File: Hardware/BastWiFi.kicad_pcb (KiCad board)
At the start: 2 copper layers, 50.8 x 22.9 mm, 31 parts, among them J1 Conn_Battery, J2 USB_B_Micro, J3 Conn_Left, J4 Conn_Right, Q1 DMG3415U-7, SW1 GPIO0, SW2 RESET, U1 MCP73831-3-OT, U2 AP2112K-3.3, U3 ESP32-S2-WROVER

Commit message: Change footprint sw
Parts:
- SW1, SW2: footprint Button_Switch_SMD:SW_SPST_TL3342 -> Button_Switch_SMD:SW_SPST_B3U-1000P
- moved REF** 9.87 mm to (185.1, 83.2)
- moved REF** 9.81 mm to (185.1, 102.2)
- moved SW1 5.97 mm to (139.0, 111.5)
- moved SW2 2.81 mm to (144.8, 111.5)
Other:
- board size 50.8 x 22.9 mm -> 60 x 22.9 mm
- net class Default: trace_width 0.25 -> 0.3

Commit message: Tracks
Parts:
- moved R1 19.9 mm to (150.1, 84.6), turned to 180 degrees
- moved SW1 17.1 mm to (136.9, 94.6)
- moved R8 16.7 mm to (141.2, 100.7), turned to 180 degrees
- moved SW2 14.4 mm to (136.9, 99.6)
- moved C6 12.8 mm to (148.0, 99.8), turned to 90 degrees
- moved D2 11.7 mm to (144.3, 88.6)
- moved U1 10.7 mm to (147.9, 87.5)
- moved C7 10.2 mm to (141.2, 99.1)
- moved C2 8.95 mm to (143.9, 93.9), turned to 270 degrees
- moved R6 8.41 mm to (132.2, 99.6), turned to 90 degrees
- moved Q1 7.22 mm to (141.3, 94.4), turned to 270 degrees
- moved U2 6.79 mm to (147.9, 95.7)
- moved C5 6.30 mm to (149.6, 99.8), turned to 90 degrees
- moved R5 6.26 mm to (133.7, 99.6), turned to 90 degrees
- moved R4 6.22 mm to (148.0, 93.1), turned to 180 degrees
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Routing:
- net /~RST~: track 0.00 -> 68.7 mm, vias 0 -> 2
- net /GPIO0: track 0.00 -> 49.5 mm, vias 0 -> 2
- net /SCL: track 0.00 -> 48.3 mm, vias 0 -> 1
- net /SDA: track 0.00 -> 44.5 mm
- net /A0: track 0.00 -> 40.0 mm, vias 0 -> 1
- net /A1: track 0.00 -> 36.8 mm, vias 0 -> 1
- net +BATT: track 0.00 -> 34.9 mm
- net /A2: track 0.00 -> 33.7 mm, vias 0 -> 1
- net /A3: track 0.00 -> 30.8 mm, vias 0 -> 1
- net /A4: track 0.00 -> 27.3 mm, vias 0 -> 1
- net /A5: track 0.00 -> 22.3 mm, vias 0 -> 1
- net VBUS: track 0.00 -> 20.1 mm
- net +3V3: track 0.00 -> 18.8 mm
- net /EN: track 0.00 -> 18.7 mm, vias 0 -> 1
- net /MISO: track 0.00 -> 8.12 mm, vias 0 -> 1
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
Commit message: Add connector
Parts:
- removed J2: USB_B_Micro, Connector_USB:USB_Micro-B_Molex-105017-0001
- added P1: USB_C_Plug_USB2.0, Connectors EC:C393939, F.Cu at (132.5, 92.5)
- moved C2 1.34 mm to (145.2, 93.7)
- moved C4 1.34 mm to (145.2, 97.1)
- moved C6 0.74 mm to (147.6, 99.2)
- moved C5 0.74 mm to (149.1, 99.2)
- moved C3 0.52 mm to (150.6, 87.3)
- moved R7 0.50 mm to (150.8, 93.3)
- moved R2 0.46 mm to (137.4, 90.7)
- moved SW1 0.27 mm to (137.1, 94.7)
- moved C7 0.24 mm to (141.0, 99.2)
- moved R8 0.24 mm to (141.0, 100.8)
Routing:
- net +3V3: track 18.8 -> 58.2 mm, vias 0 -> 4
- net /D-: track 0.00 -> 35.2 mm
- net /D+: track 0.00 -> 34.9 mm
- net VBUS: track 20.1 -> 49.6 mm, vias 0 -> 1
- net Net-(P1-PadA5): track 0.00 -> 9.64 mm, vias 0 -> 2
- net Net-(P1-PadB5): track 0.00 -> 6.57 mm
- net (no net): track 0.00 -> 6.04 mm
- net /A5: track 22.3 -> 26.0 mm
- net GND: track 5.80 -> 3.27 mm

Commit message: Route
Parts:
- moved D2 0.16 mm to (144.2, 88.4), turned to 180 degrees
- moved R3 0.11 mm to (144.3, 85.8), turned to 180 degrees
- turned R1 to 0 degrees
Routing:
- net GND: track 3.27 -> 81.6 mm, vias 0 -> 14
- net Net-(P1-PadS1): track 0.00 -> 16.9 mm
- net Net-(R3-Pad1): track 5.10 -> 2.07 mm
- net Net-(R1-Pad1): track 2.93 -> 2.01 mm
- net /SCL: track 48.3 -> 47.5 mm
- net /SDA: track 44.5 -> 43.7 mm
- net /GPIO0: track 49.5 -> 49.0 mm
- added copper zone on B.Cu, net GND
- added copper zone on F.Cu, net GND

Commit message: Change tracks
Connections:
- J3 pad 10: /A5 -> /A0
- J3 pad 5: /A0 -> /A5
- J3 pad 6: /A1 -> /A4
- J3 pad 7: /A2 -> /A3
- J3 pad 8: /A3 -> /A2
- J3 pad 9: /A4 -> /A1
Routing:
- net /A0: track 40.3 -> 30.1 mm
- net /A1: track 37.1 -> 29.7 mm
- net /A5: track 26.0 -> 33.1 mm
- net /A4: track 27.3 -> 32.6 mm
- net /~RST~: track 68.5 -> 73.5 mm
- net /A2: track 34.1 -> 29.3 mm
- net /GPIO06: track 3.52 -> 8.08 mm
- net VBUS: track 49.6 -> 54.2 mm
- net /GPIO05: track 4.82 -> 9.08 mm
- net /GPIO0: track 49.0 -> 53.0 mm
- net GND: track 81.6 -> 85.2 mm
- net /RX: track 4.44 -> 7.55 mm
- net /MISO: track 8.12 -> 11.1 mm
- net +3V3: track 58.5 -> 60.6 mm
- net /A3: track 30.8 -> 32.5 mm
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
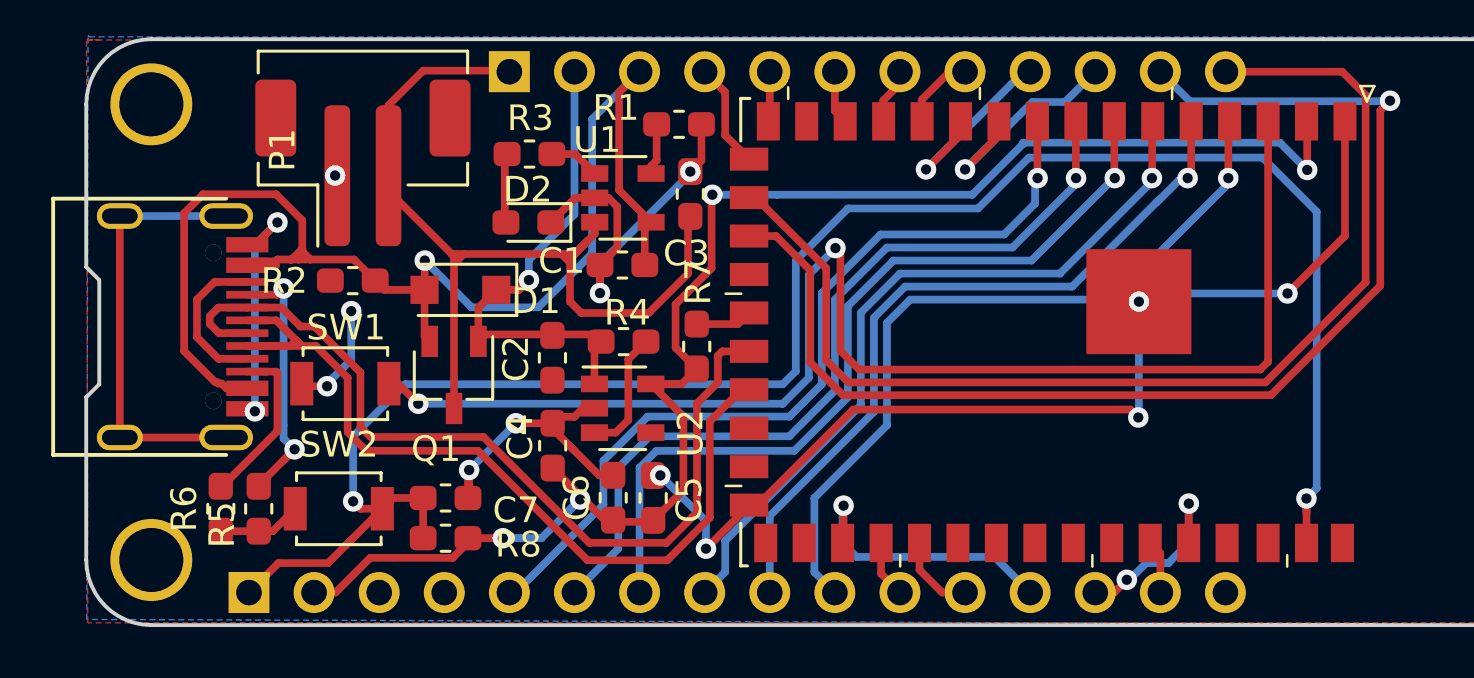
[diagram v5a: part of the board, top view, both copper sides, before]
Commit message: Add button
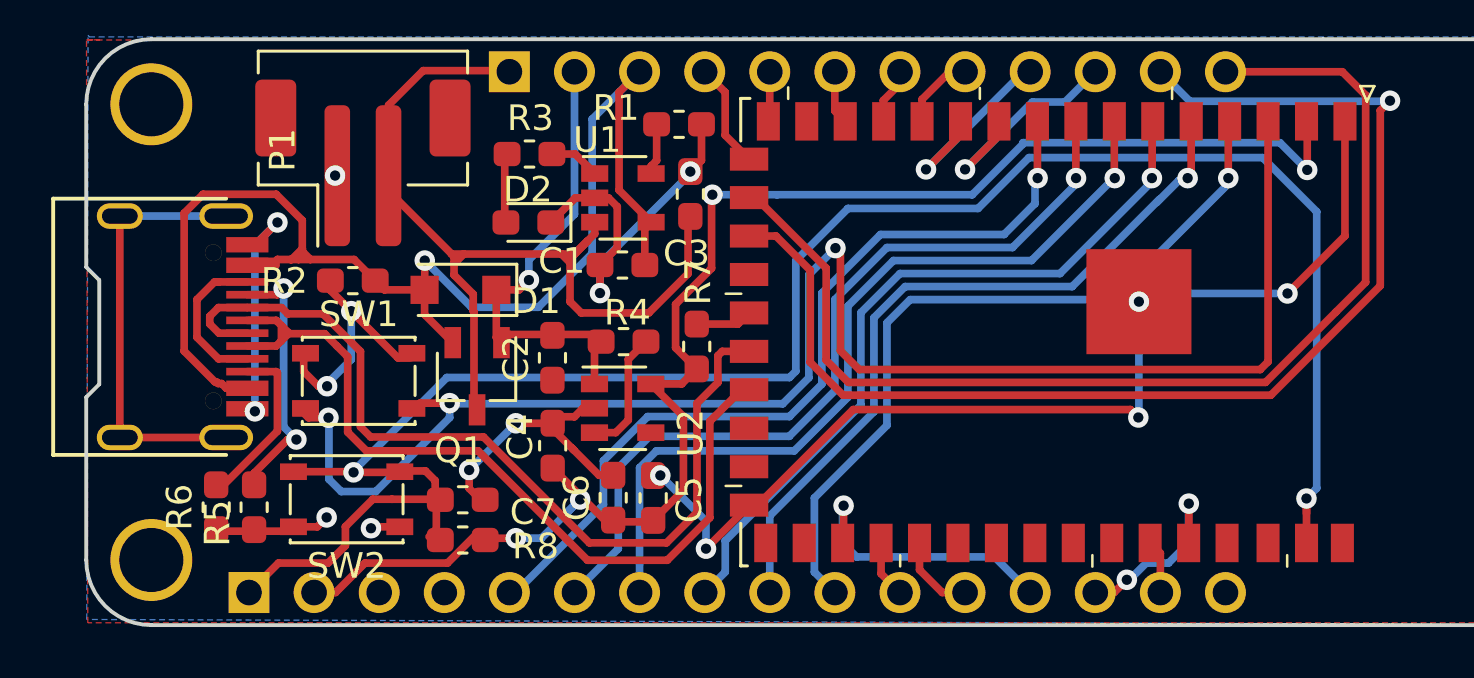
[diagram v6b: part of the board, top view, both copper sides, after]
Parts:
- SW1, SW2: footprint Button_Switch_SMD:SW_SPST_B3U-1000P -> Button_Switch_SMD:SW_SPST_PTS810
- moved Q1 0.90 mm to (142.2, 94.4)
- moved C7 0.67 mm to (141.7, 99.2)
- moved R8 0.67 mm to (141.7, 100.8)
- moved SW1 0.53 mm to (137.6, 94.6)
- moved SW2 0.48 mm to (137.2, 99.2), turned to 180 degrees
- moved R6 0.19 mm to (132.1, 99.5)
- moved R5 0.19 mm to (133.6, 99.5)
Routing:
- net /GPIO0: track 53.0 -> 62.1 mm, vias 2 -> 3
- net GND: track 85.2 -> 92.1 mm, vias 14 -> 16
- net /~RST~: track 73.5 -> 77.0 mm
- net /D+: track 33.9 -> 32.4 mm
- net /EN: track 19.6 -> 18.5 mm

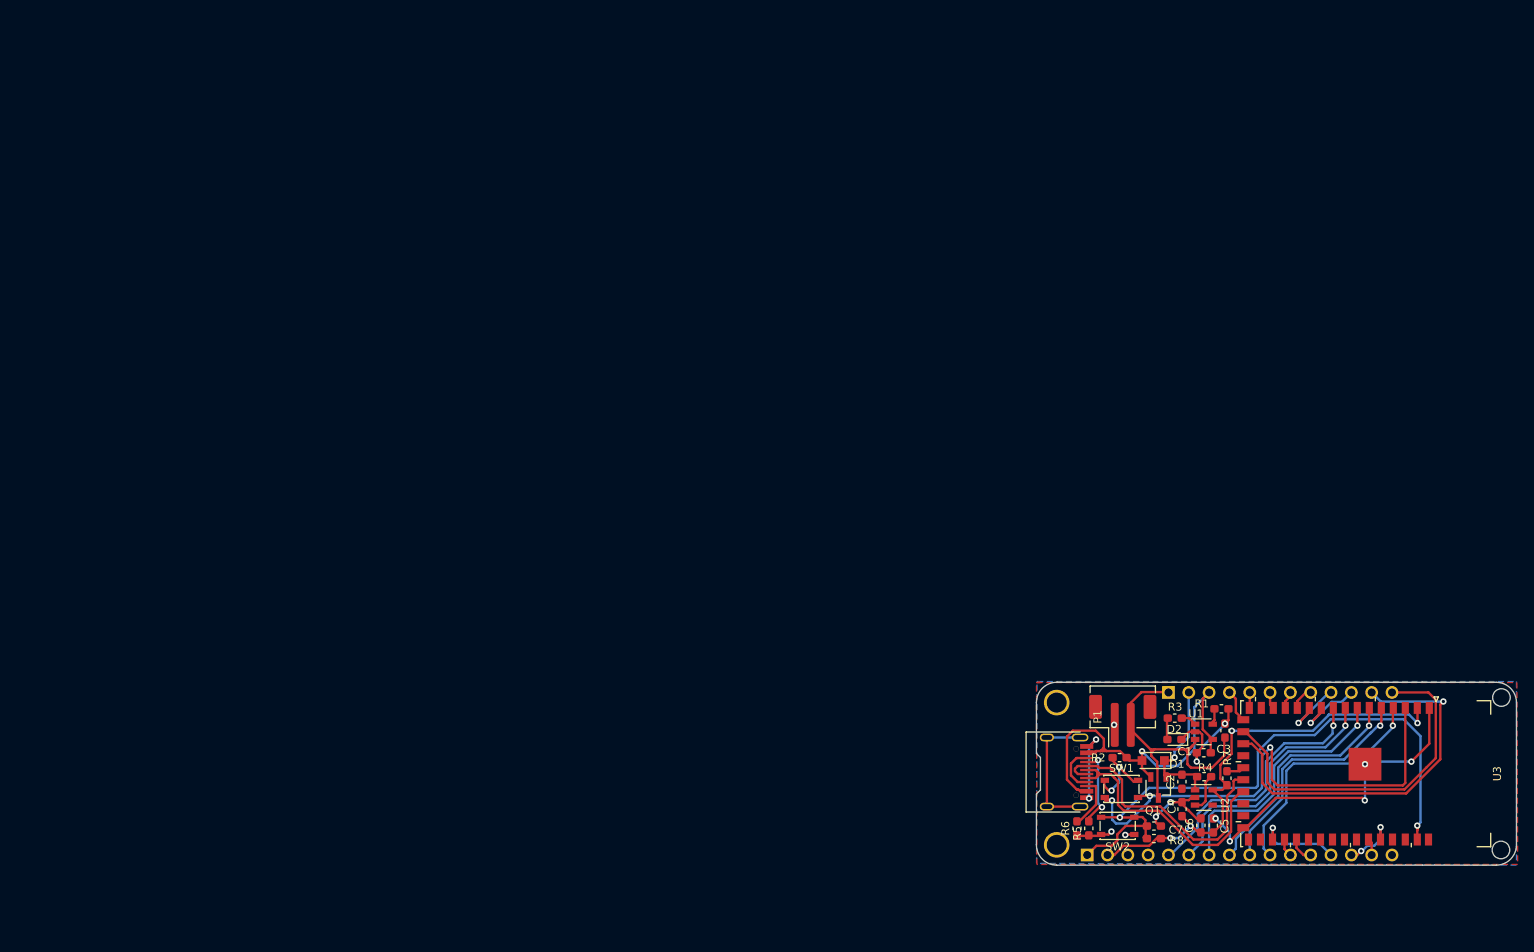
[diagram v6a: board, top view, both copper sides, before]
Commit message: Change button
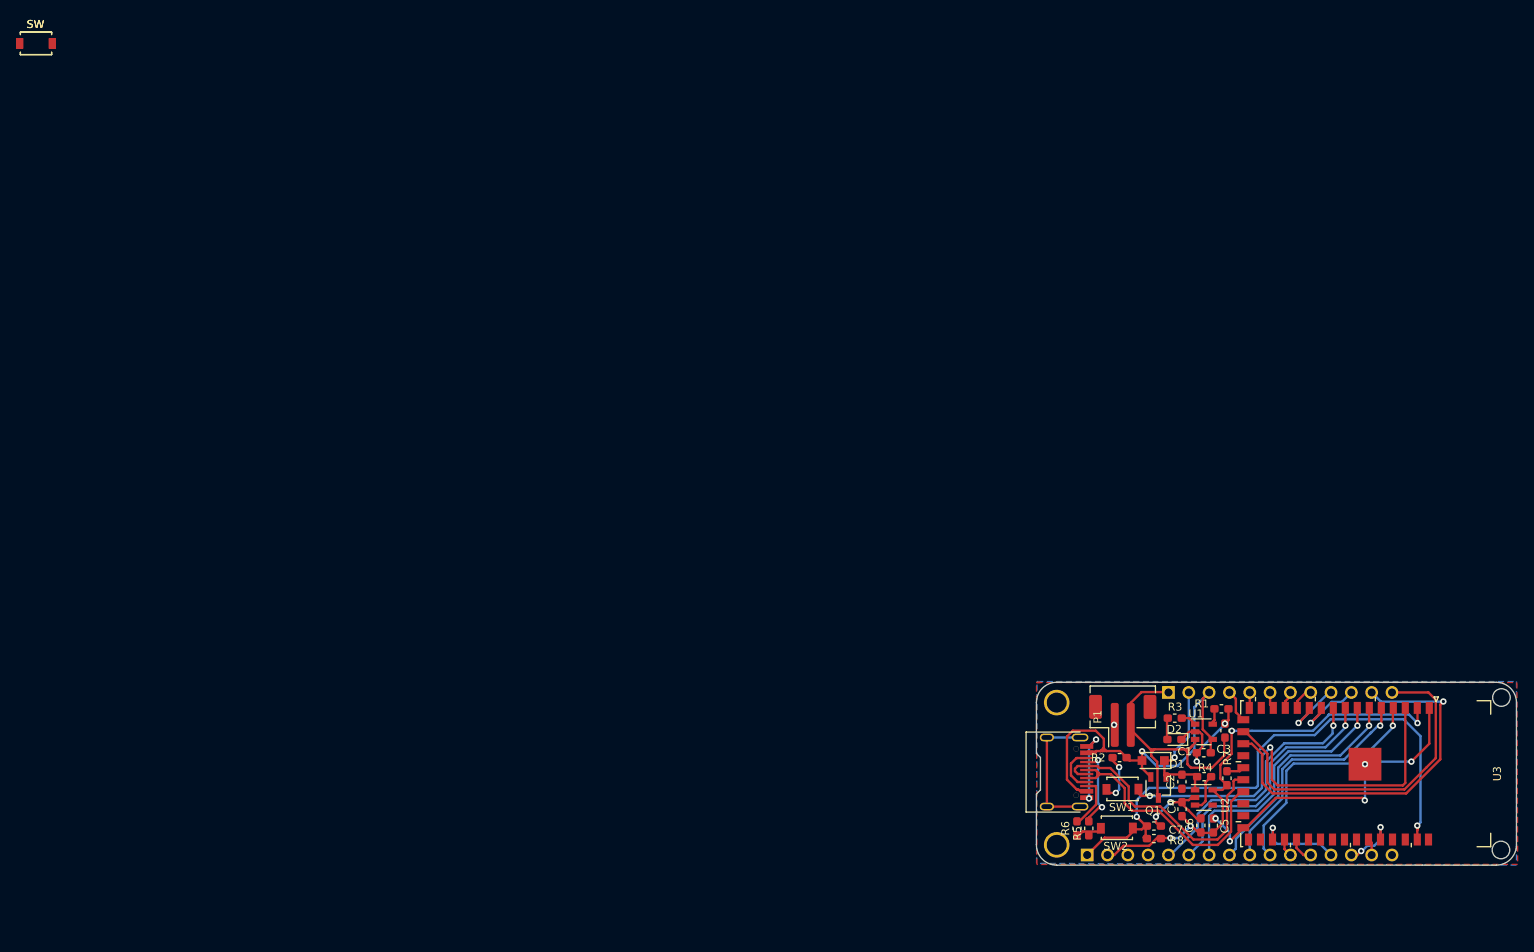
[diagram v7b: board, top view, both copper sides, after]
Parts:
- added SW (x2): C455281, Connectors EC:C455281, F.Cu at (0.00, 0.00)
- SW1, SW2: footprint Button_Switch_SMD:SW_SPST_PTS810 -> Connectors EC:C45281
- moved SW1 2.55 mm to (139.7, 96.1), turned to 180 degrees
- moved SW2 2.52 mm to (139.0, 100.9)
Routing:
- net /GPIO0: track 62.1 -> 52.0 mm, vias 3 -> 2
- net /~RST~: track 77.0 -> 70.8 mm
- net GND: track 92.1 -> 86.7 mm, vias 16 -> 14
- net /D-: track 34.8 -> 34.1 mm
- net /D+: track 32.4 -> 31.8 mm

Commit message: Change footprint
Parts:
- removed SW (x2): C455281, Connectors EC:C455281
- SW1, SW2: footprint Connectors EC:C45281 -> Connectors EC:C455281
- moved SW2 1.09 mm to (140.1, 101.1)
- moved SW1 0.80 mm to (140.5, 96.2)
- moved R8 0.29 mm to (142.0, 100.8)
- moved C7 0.29 mm to (142.0, 99.3)
